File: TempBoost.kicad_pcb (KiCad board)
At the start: 2 copper layers, 6 parts

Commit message: Placement again
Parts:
- added C101: 2200uF, BoostLib:CP_Elec_19x19, F.Cu at (134.6, 36.1)
- added C102: 2200uF, BoostLib:CP_Elec_19x19, F.Cu at (158.8, 36.1)
- added C103: 220uF, Capacitors_THT:CP_Radial_D12.5mm_P5.00mm, F.Cu at (177.8, 34.2)
- added C104: 100uF, Capacitors_SMD:CP_Elec_6.3x7.7, F.Cu at (190.5, 29.4)
- added C105: 1uF, Capacitors_SMD:C_0805, F.Cu at (149.6, 105.9)
- added C106: 1uF, Capacitors_SMD:C_0805, F.Cu at (149.1, 105.8)
- added C207: 6800pF, Capacitors_SMD:C_0603, F.Cu at (150.0, 104.6)
- added C208: 7500pF, Capacitors_SMD:C_0603, F.Cu at (150.2, 104.6)
- added C209: 1pF, Capacitors_SMD:C_0603, F.Cu at (150.4, 104.6)
- added C210: 1uF, Capacitors_SMD:C_0805, F.Cu at (149.8, 105.9)
- added C211: 100pF, Capacitors_SMD:C_0603_HandSoldering, F.Cu at (154.9, 105.9)
- added C212: 10uF, Capacitors_SMD:C_0805, F.Cu at (148.7, 105.8)
- added C213: 1uF, Capacitors_SMD:C_0805, F.Cu at (149.3, 105.8)
- added C215: 1uF, Capacitors_SMD:C_0805, F.Cu at (148.9, 105.8)
- added C216: 0.1uF, Capacitors_THT:C_Axial_L5.1mm_D3.1mm_P10.00mm_Horizontal, F.Cu at (153.5, 105.2)
- added C217: 10uF, Capacitors_THT:C_Disc_D5.0mm_W2.5mm_P2.50mm, F.Cu at (155.5, 104.8)
- added C218: 3.3uF, Capacitors_THT:C_Disc_D5.0mm_W2.5mm_P2.50mm, F.Cu at (155.7, 104.8)
- added C219: 50pF, Capacitors_SMD:C_0603, F.Cu at (150.6, 104.6)
- added D101: D_TVS, BoostLib:SMAJ40ALFCT, F.Cu at (118.1, 33.0)
- added D201: D, BoostLib:RFN10BM3SFHTL, F.Cu at (146.1, 57.1)
- added D204: D_TVS, BoostLib:SMAJ40ALFCT, F.Cu at (177.1, 47.0)
- added D205: D_TVS, BoostLib:SMAJ40ALFCT, F.Cu at (143.5, 77.5)
- added F101: Fuse, SMD_Packages:SMD-1206_Pol, F.Cu at (58.4, 39.4)
- added J1: Conn_01x02, ED1202DS:ED1202DS, F.Cu at (52.1, 49.5)
- added J2: Conn_01x02, ED1202DS:ED1202DS, F.Cu at (52.1, 95.2)
- added L1: 2.2mH, BoostLib:1140-122K, F.Cu at (160.3, 72.4)
- added Q201: Q_NMOS_GSD, TO_SOT_Packages_SMD:SOT-23, F.Cu at (146.3, 70.2)
- added R1: 33, Resistors_THT:R_Axial_DIN0614_L14.3mm_D5.7mm_P20.32mm_Horizontal, F.Cu at (148.5, 104.7)
- added R201: 118K, Resistors_SMD:R_0805, F.Cu at (152.5, 105.6)
- added R202: 10K, Resistors_SMD:R_0805, F.Cu at (152.9, 105.7)
- added R203: 130k, Resistors_SMD:R_0603, F.Cu at (146.8, 105.3)
- added R204: 3k, Resistors_SMD:R_0603, F.Cu at (147.0, 105.3)
- added R205: 10k, Resistors_SMD:R_0805, F.Cu at (150.8, 105.4)
- added R206: 10k, Resistors_SMD:R_0805, F.Cu at (151.0, 105.4)
- added R207: 60.4k, Resistors_SMD:R_0805, F.Cu at (151.3, 105.5)
- added R208: 10k, Resistors_SMD:R_0805, F.Cu at (182.9, 40.6)
- added R209: 10K, Resistors_SMD:R_0805, F.Cu at (151.5, 105.5)
- added R210: 10M, Resistors_SMD:R_0805, F.Cu at (151.7, 105.5)
- added R211: 470K, Resistors_SMD:R_0603, F.Cu at (147.2, 105.4)
- added R212: 27K, Resistors_SMD:R_0603, F.Cu at (147.4, 105.4)
- added R213: 10K, Resistors_SMD:R_0805, F.Cu at (151.9, 105.6)
- added R214: 330, Resistors_SMD:R_0805, F.Cu at (182.9, 46.6)
- added R215: 330, Resistors_SMD:R_0805, F.Cu at (182.9, 43.6)
- added R216: 47K, Resistors_SMD:R_0603, F.Cu at (146.6, 105.3)
- added R217: 1M, Resistors_SMD:R_0603, F.Cu at (147.6, 105.4)
- added RV1: POT, Potentiometers:Potentiometer_Trimmer_Bourns_3296W, F.Cu at (148.7, 105.3)
- added RV2: 5k, Potentiometers:Potentiometer_Trimmer_Bourns_3296W, F.Cu at (148.5, 105.2)
- added SW101: SW_SPST, 400MSP1R6BLKM6QE:400MSP1R6BLKM6QE, F.Cu at (54.6, 26.7)
- added T101: 3FD-224, 3FD-224:3FD-224, F.Cu at (81.3, 41.3)
- added U101: DF005S2, BoostLib:DF10S2, F.Cu at (108.0, 30.5)
- added U201: MIC2920, TO_SOT_Packages_SMD:SOT-223-3_TabPin2, F.Cu at (155.9, 105.1)
- added U203: UCC27517A, TO_SOT_Packages_SMD:SOT-23-5, F.Cu at (155.3, 105.1)
- added U204: 2925, TO_SOT_Packages_SMD:SOT-23, F.Cu at (155.5, 105.1)
- added U205: LM2904, Housings_SOIC:SOIC-8_3.9x4.9mm_Pitch1.27mm, F.Cu at (153.6, 104.9)
- added U206: TPS1H100, Housings_SSOP:TSSOP-14-1EP_4.4x5mm_Pitch0.65mm, F.Cu at (190.5, 45.7)
- added U207: LM1117-5.0, TO_SOT_Packages_SMD:SOT-223-3_TabPin2, F.Cu at (156.1, 105.2)
- added U208: MAX4477, Housings_SOIC:SOIC-8_3.9x4.9mm_Pitch1.27mm, F.Cu at (154.6, 105.0)
- C201, C202: value 100u -> 100uF; footprint Capacitors_SMD:C_0805 -> Capacitors_SMD:CP_Elec_6.3x7.7
- C203, C204: value 10u -> 10uF
- C205, C206: value 1u -> 1uF
- moved C206 89.4 mm to (61.0, 87.9), turned to 90 degrees
- moved C205 89.2 mm to (61.0, 94.0)
- moved C204 81.9 mm to (64.8, 87.9), turned to 90 degrees
- moved C203 81.6 mm to (64.8, 94.2)
- moved C202 72.7 mm to (71.1, 85.1), turned to 90 degrees
- moved C201 71.2 mm to (71.1, 96.5), turned to 270 degrees
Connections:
- C202 pad 1: Net-(C201-Pad1) -> Net-(C202-Pad1)
- C202 pad 2: Net-(C201-Pad2) -> Net-(C202-Pad2)
- C203 pad 1: Net-(C201-Pad1) -> Net-(C203-Pad1)
- C203 pad 2: Net-(C201-Pad2) -> Net-(C203-Pad2)
- C204 pad 1: Net-(C201-Pad1) -> Net-(C204-Pad1)
- C204 pad 2: Net-(C201-Pad2) -> Net-(C204-Pad2)
- C205 pad 1: Net-(C201-Pad1) -> Net-(C205-Pad1)
- C205 pad 2: Net-(C201-Pad2) -> Net-(C205-Pad2)
- C206 pad 1: Net-(C201-Pad1) -> Net-(C206-Pad1)
- C206 pad 2: Net-(C201-Pad2) -> Net-(C206-Pad2)
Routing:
- removed copper zone on F.Cu, net Net-(C201-Pad2)
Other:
- board text added: "HV Keepout"

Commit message: Base Placement
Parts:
- C202: value 100uF -> 100uf
- L1: value 2.2mH -> L; footprint BoostLib:1140-122K -> 1140-122K
- moved R211 111.4 mm to (38.2, 82.6), turned to 180 degrees
- moved R213 105.9 mm to (48.3, 83.8), turned to 180 degrees
- moved RV2 105.0 mm to (45.7, 83.8), turned to 270 degrees
- moved C218 104.7 mm to (52.0, 90.2), turned to 180 degrees
- moved RV1 103.4 mm to (45.7, 96.5), turned to 270 degrees
- moved C217 102.5 mm to (53.3, 96.5), turned to 180 degrees
- moved R212 95.7 mm to (54.6, 82.0), turned to 270 degrees
- moved U208 93.9 mm to (63.3, 83.0), turned to 180 degrees
- moved D201 93.7 mm to (74.9, 118.1), turned to 180 degrees
- moved R217 93.5 mm to (57.1, 82.0), turned to 270 degrees
- moved R209 89.4 mm to (63.8, 87.6), turned to 180 degrees
- moved C216 88.7 mm to (66.0, 90.2), turned to 180 degrees
- moved R216 86.0 mm to (64.8, 78.7), turned to 180 degrees
- moved C219 83.3 mm to (69.8, 84.3), turned to 90 degrees
- moved R210 81.3 mm to (73.3, 83.8)
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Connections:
- net Gate renamed GATE
- net Net-(C213-Pad1) renamed /Ref_in
- net Net-(F101-Pad2) renamed /AC_fused
- net Net-(J1-Pad1) renamed /AC_Com
- net Net-(R207-Pad2) renamed /OV_Set
- net Net-(R214-Pad2) renamed /TI_CL
- net Net-(R215-Pad2) renamed /TI_CS
- net Net-(T101-Pad5) renamed /AC+
- net Net-(T101-Pad8) renamed /AC-
- C101 pad 2: VRECT- -> GND
- C102 pad 2: VRECT- -> GND
- C103 pad 2: VRECT- -> GND
- C104 pad 2: VRECT- -> GND
- C201 pad 1: Net-(C201-Pad1) -> LOAD+
- C201 pad 2: Net-(C201-Pad2) -> GND
- C202 pad 1: Net-(C202-Pad1) -> LOAD+
- C202 pad 2: Net-(C202-Pad2) -> GND
- C203 pad 1: Net-(C203-Pad1) -> LOAD+
- C203 pad 2: Net-(C203-Pad2) -> GND
- C204 pad 1: Net-(C204-Pad1) -> LOAD+
- C204 pad 2: Net-(C204-Pad2) -> GND
- C205 pad 1: Net-(C205-Pad1) -> LOAD+
- C205 pad 2: Net-(C205-Pad2) -> GND
- C206 pad 1: Net-(C206-Pad1) -> LOAD+
- C206 pad 2: Net-(C206-Pad2) -> GND
- C210 pad 2: VRECT- -> Net-(C210-Pad2)
- C211 pad 2: VRECT- -> Net-(C210-Pad2)
- C212 pad 2: VRECT- -> Net-(C210-Pad2)
- D101 pad 2: VRECT- -> GND
- D201 pad 1: Net-(D201-Pad1) -> LOAD+
- D201 pad 2: Net-(D201-Pad2) -> /I_Side
- D204 pad 1: Net-(D204-Pad1) -> VSWITCHED
- D204 pad 2: Net-(D204-Pad2) -> /I_Side
- D205 pad 1: Net-(D205-Pad1) -> VSWITCHED
- D205 pad 2: Net-(D205-Pad2) -> GND
- Q201 pad 3: Net-(Q201-Pad3) -> /I_Side
- U101 pad 2: VRECT- -> GND
- U203 pad 2: VRECT- -> GND
- U203 pad 4: VRECT- -> GND
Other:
- board outline added: 106.7 x 101.6 mm
- board text added: "R1 = optional gate resistor? Change to 33 Ohm 0805 if I can change the BOM"

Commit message: Starting Layout
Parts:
- moved C210 1.16 mm to (107.1, 49.5)
- moved C201 0.64 mm to (66.0, 116.2)
- moved C202 0.64 mm to (66.0, 104.8)
- moved C204 0.63 mm to (59.7, 107.6)
- moved C206 0.63 mm to (55.9, 107.6)
- moved C105 0.47 mm to (105.4, 65.7)
- moved C212 0.25 mm to (103.1, 49.5)
- turned C203 to 270 degrees
- turned C205 to 270 degrees
- turned U206 to 90 degrees
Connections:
- C210 pad 2: Net-(C210-Pad2) -> GND
- C211 pad 2: Net-(C210-Pad2) -> GND
- C212 pad 2: Net-(C210-Pad2) -> GND
- J1 pad 1: /AC_Com -> Net-(J1-Pad1)
- J1 pad 2: Net-(J1-Pad2) -> /AC_Com
- SW101 pad 1: Net-(J1-Pad2) -> Net-(J1-Pad1)
- U201 pad 2: Net-(U201-Pad2) -> GND
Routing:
- net /AC_Com: track 0.00 -> 29.8 mm
- net GND: track 0.00 -> 28.8 mm, vias 0 -> 4
- net /AC-: track 0.00 -> 22.5 mm
- net VRECT+: track 0.00 -> 22.1 mm
- net /AC_fused: track 0.00 -> 20.1 mm
- net Net-(J1-Pad1): track 0.00 -> 15.2 mm
- net LOAD+: track 0.00 -> 14.9 mm
- net Net-(F101-Pad1): track 0.00 -> 9.41 mm
- net /AC+: track 0.00 -> 8.56 mm
- net Net-(T101-Pad6): track 0.00 -> 6.35 mm
- net +12V: track 0.00 -> 5.29 mm
- added copper zone on B.Cu, net GND
- added copper zone on F.Cu, net LOAD+
- added copper zone on F.Cu, net VRECT+
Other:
- net class 120V added: clearance 1, trace_width 1, via_dia 0.6, via_drill 0.4

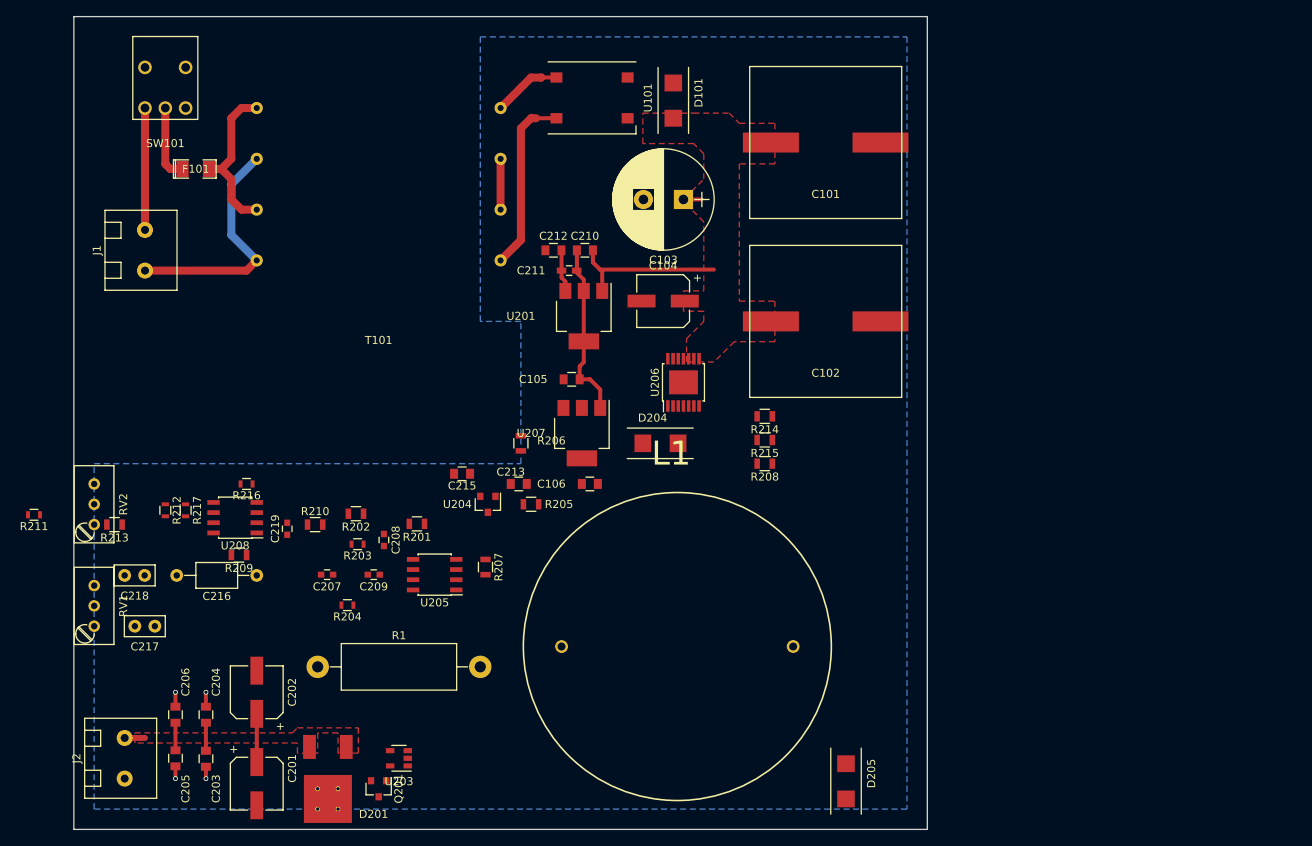
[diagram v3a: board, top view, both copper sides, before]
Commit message: More Routing
PWM Generator is routed so that it now works but the freqency is 70Hz rather than 70k. RIP
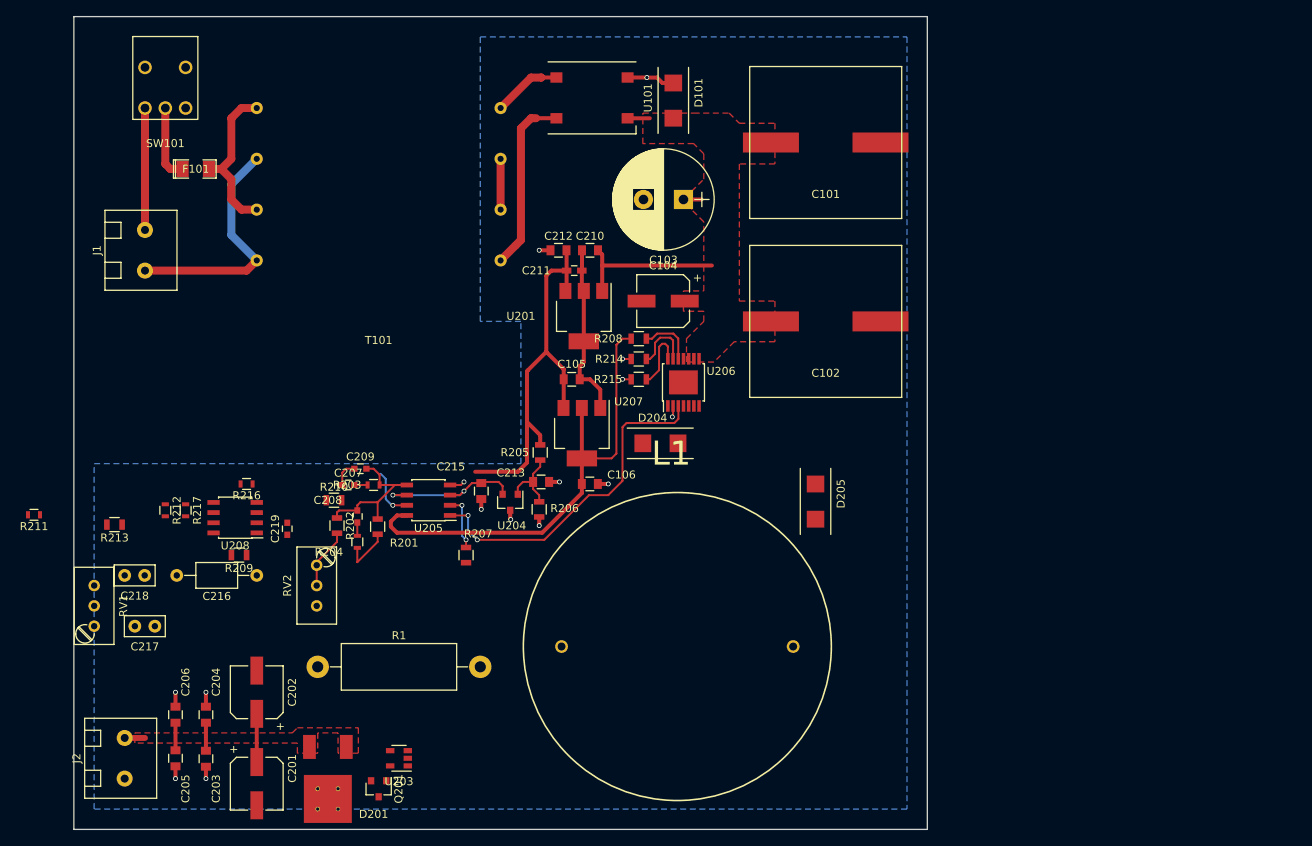
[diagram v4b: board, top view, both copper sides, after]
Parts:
- moved D205 35.2 mm to (135.9, 83.1)
- moved RV2 28.3 mm to (73.5, 88.9), turned to 90 degrees
- moved R208 22.2 mm to (113.8, 60.6), turned to 0 degrees
- moved R215 17.5 mm to (113.8, 65.7), turned to 0 degrees
- moved R214 17.3 mm to (113.8, 63.1), turned to 0 degrees
- moved C209 13.3 mm to (79.0, 76.8), turned to 0 degrees
- moved C207 11.5 mm to (77.5, 78.9), turned to 0 degrees
- moved U205 9.34 mm to (87.5, 80.8)
- moved R206 8.57 mm to (101.3, 81.9), turned to 270 degrees
- moved R204 8.00 mm to (78.6, 86.0), turned to 270 degrees
- moved R203 7.67 mm to (80.6, 78.9), turned to 0 degrees
- moved R205 6.58 mm to (101.5, 74.8), turned to 270 degrees
- moved R201 4.92 mm to (81.2, 84.1), turned to 270 degrees
- moved C208 4.44 mm to (78.6, 82.8)
- moved R210 3.85 mm to (75.7, 80.8)
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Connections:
- C213 pad 2: Net-(C213-Pad2) -> GND
- RV2 pad 1: Net-(RV2-Pad1) -> Net-(R202-Pad2)
- RV2 pad 2: Net-(RV2-Pad2) -> Net-(R202-Pad2)
- RV2 pad 3: Net-(RV2-Pad3) -> GND
- U205 pad 5: Net-(U205-Pad5) -> Net-(C208-Pad1)
- U205 pad 7: Net-(U205-Pad7) -> VFB
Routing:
- net +5V: track 0.00 -> 60.2 mm
- net +12V: track 5.29 -> 50.7 mm
- net OVSD: track 0.00 -> 42.8 mm, vias 0 -> 2
- net VREF: track 0.00 -> 19.3 mm, vias 0 -> 2
- net GND: track 28.8 -> 47.8 mm, vias 4 -> 15
- net Net-(C208-Pad1): track 0.00 -> 18.5 mm
- net VFB: track 0.00 -> 9.65 mm, vias 0 -> 1
- net /Ref_in: track 0.00 -> 8.97 mm
- net /TI_CS: track 0.00 -> 7.92 mm
- net /TI_CL: track 0.00 -> 7.69 mm
- net Net-(R202-Pad2): track 0.00 -> 7.60 mm
- net Net-(R208-Pad2): track 0.00 -> 7.03 mm
- net /OV_Set: track 0.00 -> 6.97 mm, vias 0 -> 2
- net LOAD+: track 14.9 -> 21.2 mm
- net VRECT+: track 22.1 -> 24.1 mm
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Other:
- board text added: "Vague HV Keepout"
- board text removed: "HV Keepout"

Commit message: Done
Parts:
- removed C216: 0.1uF, Capacitors_THT:C_Axial_L5.1mm_D3.1mm_P10.00mm_Horizontal
- removed C217: 10uF, Capacitors_THT:C_Disc_D5.0mm_W2.5mm_P2.50mm
- removed R209, R213: 10K, Resistors_SMD:R_0805
- added TP1: Pin_Header_Straight_1x01_Pitch2.54mm, Pin_Headers:Pin_Header_Straight_1x01_Pitch2.54mm, F.Cu at (59.7, 89.5)
- added TP2: Pin_Header_Straight_1x01_Pitch2.54mm, Pin_Headers:Pin_Header_Straight_1x01_Pitch2.54mm, F.Cu at (75.6, 73.0)
- added TP3: Pin_Header_Straight_1x01_Pitch2.54mm, Pin_Headers:Pin_Header_Straight_1x01_Pitch2.54mm, F.Cu at (85.6, 117.1)
- C218: value 3.3uF -> 22nF
- R211: value 470K -> 47K
- R212: value 27K -> 5K
- R216: value 47K -> 4.7K
- R217: value 1M -> 500k
- moved RV1 40.5 mm to (85.5, 88.9), turned to 90 degrees
- moved D204 31.5 mm to (142.2, 94.7), turned to 270 degrees
- moved R211 29.7 mm to (67.8, 85.3), turned to 0 degrees
- moved L1 20.0 mm to (118.2, 85.6), turned to 270 degrees
- moved D205 14.7 mm to (124.7, 73.7), turned to 0 degrees
- moved C218 12.8 mm to (64.3, 86.4), turned to 270 degrees
- moved R212 7.52 mm to (62.1, 81.4)
- moved R216 4.71 mm to (60.1, 78.5), turned to 270 degrees
- moved U208 4.26 mm to (67.3, 81.4)
- moved C219 3.49 mm to (72.8, 82.4)
- moved R1 3.45 mm to (73.3, 105.0)
- moved R217 2.99 mm to (60.1, 81.4)
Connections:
- Q201 pad 2: Net-(Q201-Pad2) -> GND
- R216 pad 1: INA- -> VREF
- U203 pad 3: VPWM -> OUTB
- U208 pad 2: INA- -> VREF
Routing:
- net GND: track 47.8 -> 366.0 mm, vias 15 -> 184
- net LOAD+: track 21.2 -> 90.9 mm
- net OUTB: track 0.00 -> 60.4 mm, vias 0 -> 2
- net /I_Side: track 0.00 -> 45.2 mm
- net +12V: track 50.7 -> 92.0 mm, vias 0 -> 4
- net VSWITCHED: track 0.00 -> 31.1 mm
- net VREF: track 19.3 -> 48.4 mm, vias 2 -> 4
- net +5V: track 60.2 -> 81.9 mm, vias 0 -> 2
- net Net-(R1-Pad2): track 0.00 -> 20.7 mm
- net GATE: track 0.00 -> 20.0 mm
- net INA+: track 0.00 -> 15.0 mm
- net INB-: track 0.00 -> 12.8 mm, vias 0 -> 1
- net /OV_Set: track 6.97 -> 18.5 mm
- net VFB: track 9.65 -> 19.1 mm, vias 1 -> 2
- net INB+: track 0.00 -> 6.19 mm
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- added copper zone on B.Cu, net /I_Side
- added copper zone on F.Cu, net /I_Side
- added copper zone on F.Cu, net GND
- added copper zone on F.Cu, net VSWITCHED
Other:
- board text added: "120V Keepout Isolation Region"
- board text removed: "R1 = optional gate resistor? Change to 33 Ohm 0805 if I can change the BOM"
- board text removed: "Vague HV Keepout"
